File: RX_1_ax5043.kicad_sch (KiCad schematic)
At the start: 19 parts, among them P5 CONUFL001-SMD-T, Q3 DMP2037U-7, U21 AX5043

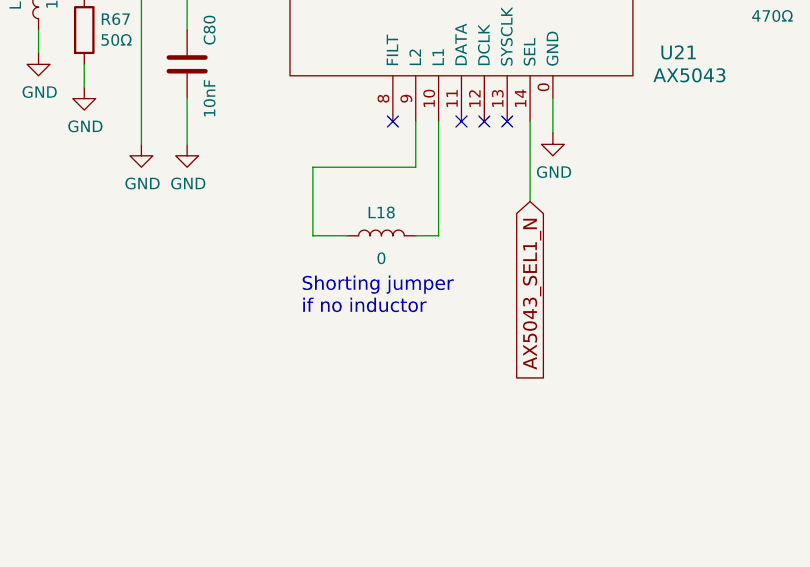
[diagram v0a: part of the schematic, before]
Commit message: Update schematics to match what is done to the boards so far
Get ready to split off a branch where the updates to the board can be
done while still keeping updates for the prototypes.

Signed-off-by: Corey Minyard <corey@minyard.net>
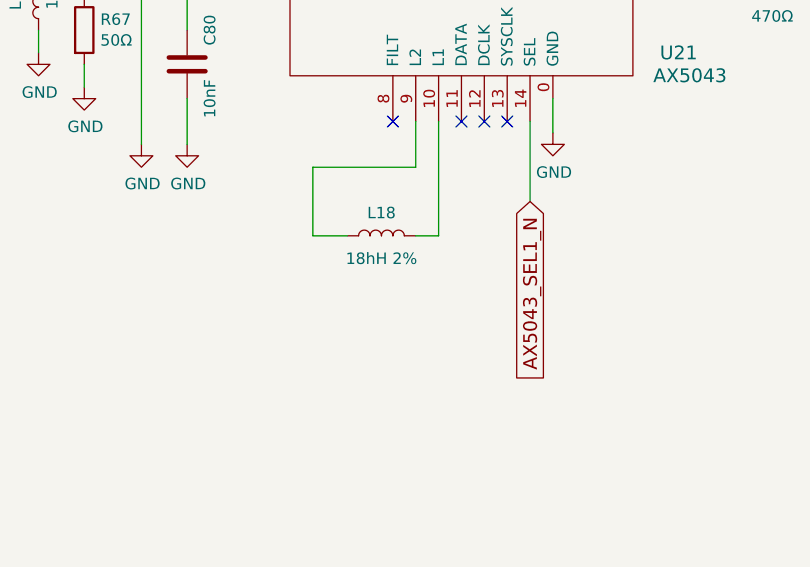
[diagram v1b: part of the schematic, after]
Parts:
- L18: value 0 -> 18hH 2%
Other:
- note removed: "Shorting jumper if no inductor"
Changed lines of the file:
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@@
-		)
-	)
-	(text "Shorting jumper\nif no inductor"
-		(exclude_from_sim no)
-		(at 203.2 181.61 0)
-		(effects
-			(font
-				(size 1.524 1.524)
-			)
-			(justify left bottom)
 		)
 	)
@@
 			)
 		)
-		(property "Value" "0"
+		(property "Value" "18hH 2%"
 			(at 212.09 175.26 90)
 			(effects

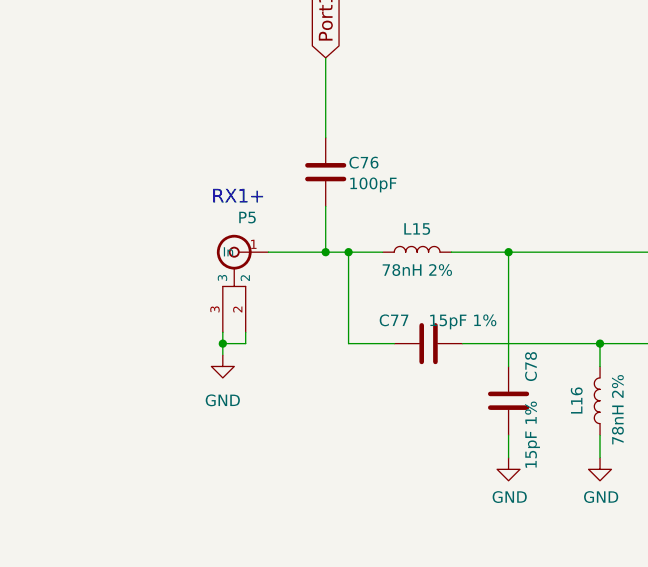
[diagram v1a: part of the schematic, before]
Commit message: Clean up the U.FL connectors a little more
Re-add the ones for TX/RX so both MMCX and U.FL are available.

Move P8 to a better location.

Signed-off-by: Corey Minyard <corey@minyard.net>
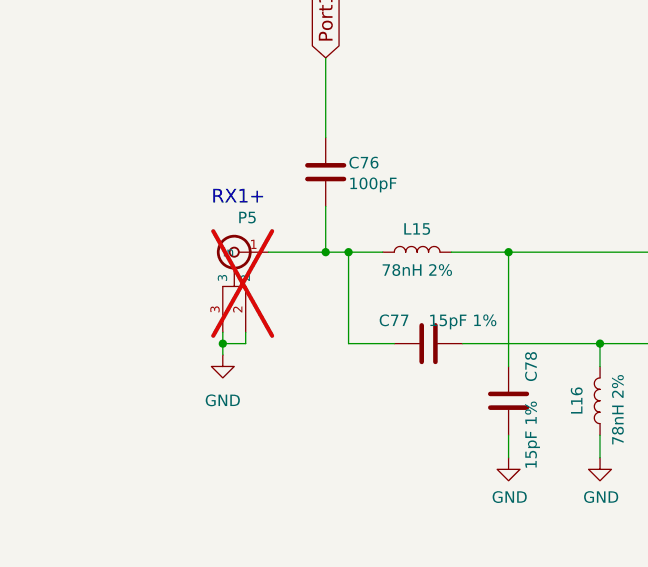
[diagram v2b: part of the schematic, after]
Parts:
- P5: now not fitted; now left out of the parts list
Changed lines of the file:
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@@
 		(unit 1)
 		(exclude_from_sim no)
-		(in_bom yes)
+		(in_bom no)
 		(on_board yes)
-		(dnp no)
+		(dnp yes)
 		(property "Reference" "P5"
 			(at 125.73 125.73 0)

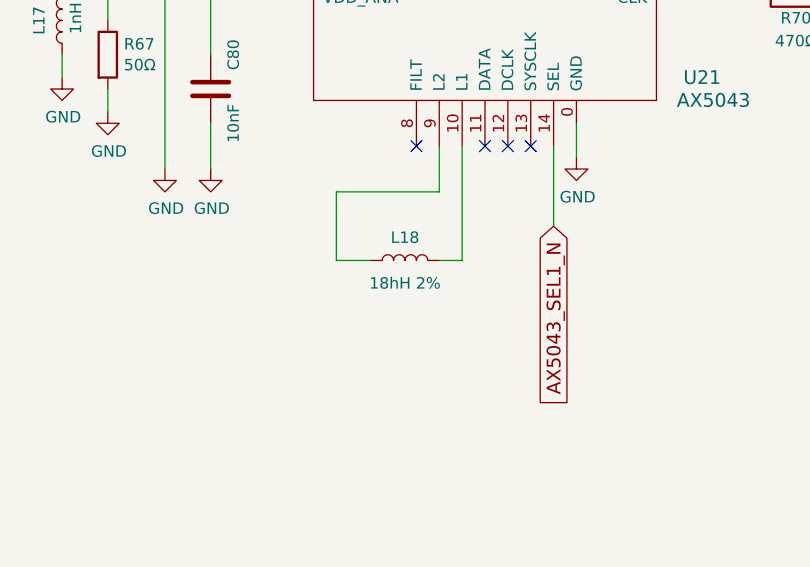
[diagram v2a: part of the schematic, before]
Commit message: Clean up BOM issues
Fix missing parts and mistypes parts.

Signed-off-by: Corey Minyard <corey@minyard.net>
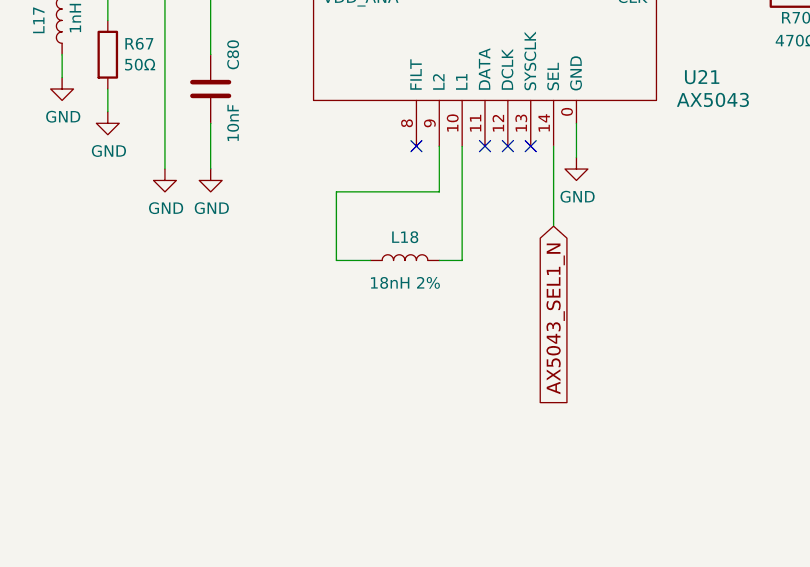
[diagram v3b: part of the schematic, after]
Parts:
- L18: value 18hH 2% -> 18nH 2%
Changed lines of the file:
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@@
 			)
 		)
-		(property "Value" "18hH 2%"
+		(property "Value" "18nH 2%"
 			(at 212.09 175.26 90)
 			(effects

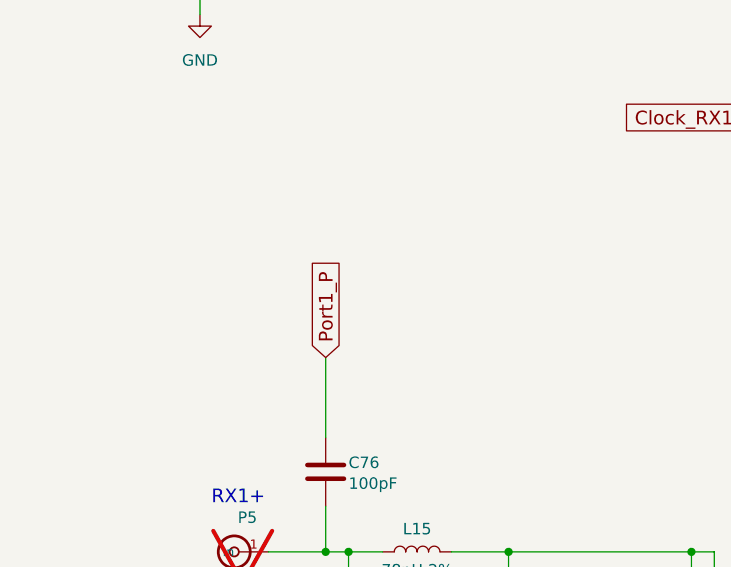
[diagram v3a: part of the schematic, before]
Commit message: Run the extra GPIOs to the PC104
They were recently freed with the ABF rework, use them.

Also, a kicad update broke some stuff, fix it.

Signed-off-by: Corey Minyard <corey@minyard.net>
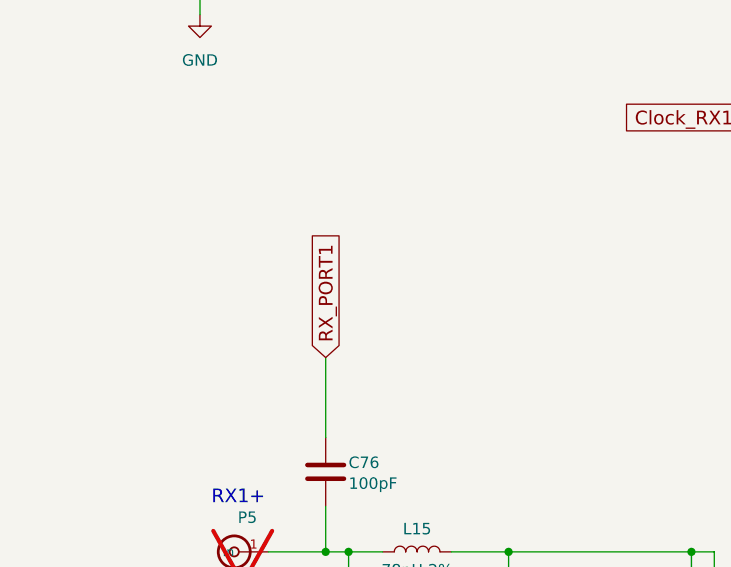
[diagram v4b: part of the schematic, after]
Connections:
- net Port1_P renamed RX_PORT1
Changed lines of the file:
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@@
 		)
 	)
-	(global_label "Port1_P"
+	(global_label "RX_PORT1"
 		(shape input)
 		(at 133.35 107.95 90)
@@
 		)
 		(property "Intersheetrefs" "${INTERSHEET_REFS}"
-			(at 133.35 96.2995 90)
+			(at 133.35 93.7596 90)
 			(effects
 				(font

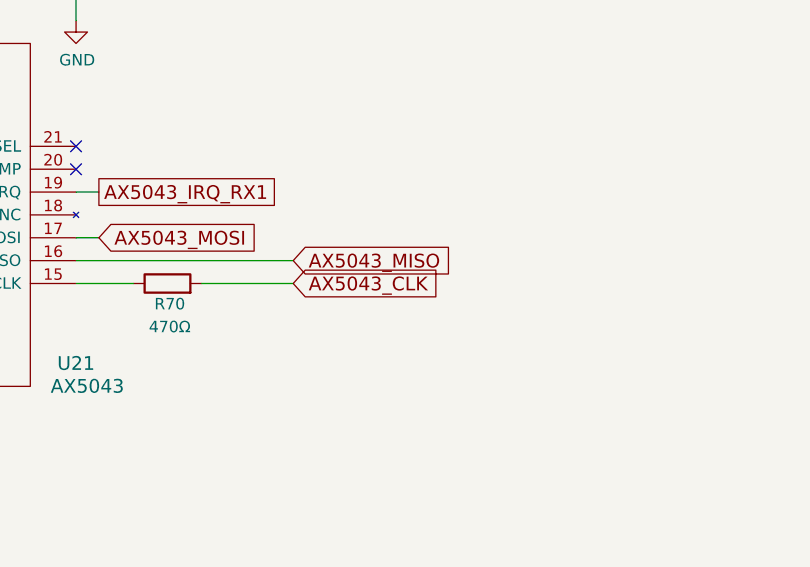
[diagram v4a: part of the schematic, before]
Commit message: Get the board ready for operation
Make the board ready as a final product, remove the lab testing portions
and add in the things required for full operation.

Signed-off-by: Corey Minyard <corey@minyard.net>
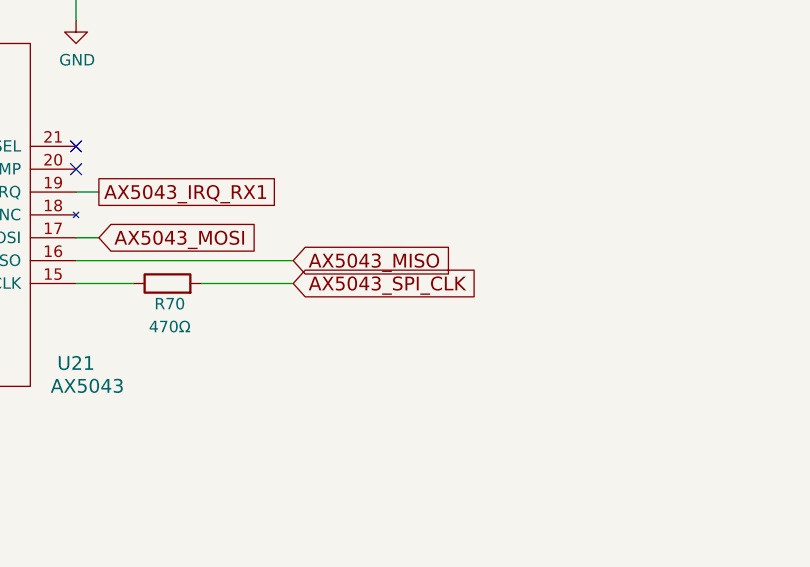
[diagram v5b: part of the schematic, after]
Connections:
- net AX5043_CLK renamed AX5043_SPI_CLK
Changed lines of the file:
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@@
 		)
 	)
-	(global_label "AX5043_CLK"
+	(global_label "AX5043_SPI_CLK"
 		(shape input)
 		(at 269.24 143.51 0)

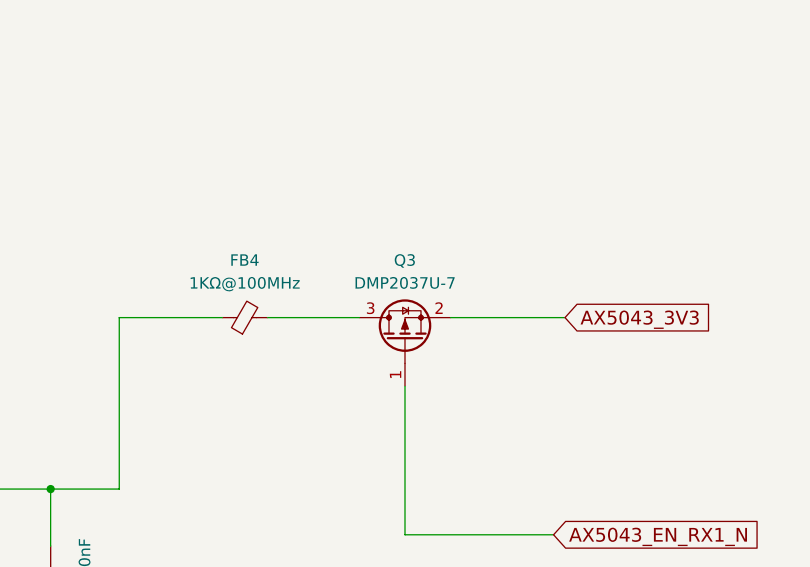
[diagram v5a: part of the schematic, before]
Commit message: Parts replacements for out of stock parts
Signed-off-by: Corey Minyard <corey@minyard.net>
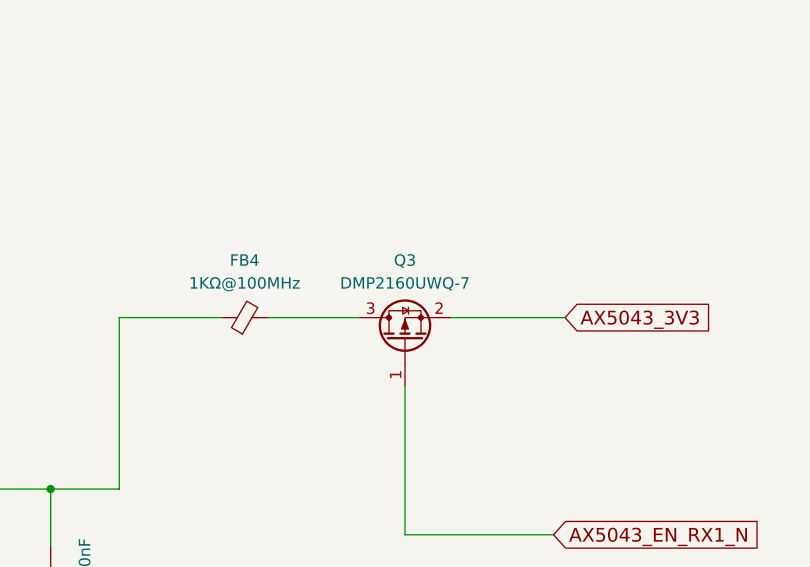
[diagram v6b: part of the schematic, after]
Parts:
- Q3: value DMP2037U-7 -> DMP2160UWQ-7; footprint Package_TO_SOT_SMD:SOT-23 -> Package_TO_SOT_SMD:SOT-323_SC-70
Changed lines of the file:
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@@
 			)
 		)
-		(property "Value" "DMP2037U-7"
+		(property "Value" "DMP2160UWQ-7"
 			(at 284.48 72.39 90)
 			(effects
@@
 			)
 		)
-		(property "Footprint" "Package_TO_SOT_SMD:SOT-23"
+		(property "Footprint" "Package_TO_SOT_SMD:SOT-323_SC-70"
 			(at 281.94 73.66 0)
 			(effects
